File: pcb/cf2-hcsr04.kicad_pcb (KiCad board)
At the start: 2 copper layers, 25.2 x 27.3 mm, 9 parts, among them P1 CF_EXP_LEFT, P2 CF_EXP_RIGHT, U1 DS28E05, U2 REG71050, U3 HC-SR04

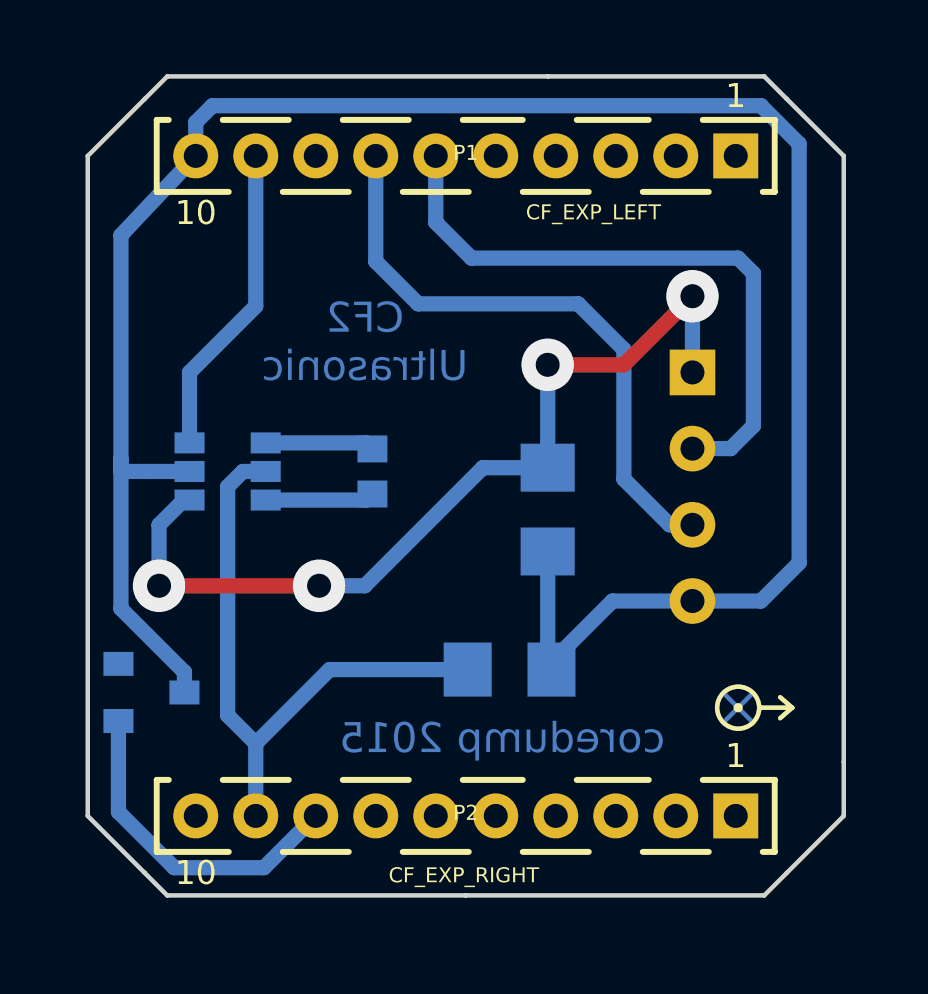
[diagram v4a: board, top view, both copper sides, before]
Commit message: Increased clearance between some vias and traces
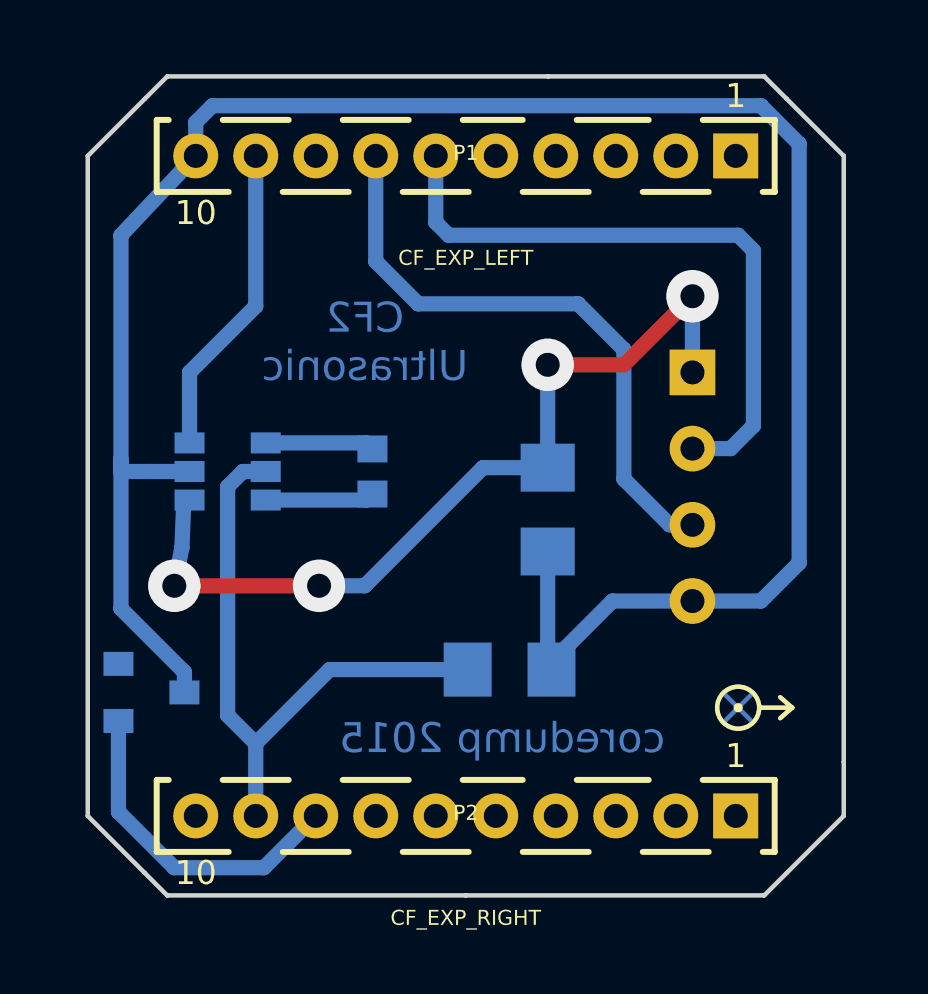
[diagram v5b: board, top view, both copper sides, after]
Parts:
- P1: footprint connectors:BF090-10-X-B2-LEFT-NOPADS -> connectors:BF090-10-X-B2-NOPADS
- P2: footprint connectors:BF090-10-X-B2-RIGHT-NOPADS -> connectors:BF090-10-X-B2-NOPADS
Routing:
- net N-0000022: track 29.7 -> 28.9 mm
